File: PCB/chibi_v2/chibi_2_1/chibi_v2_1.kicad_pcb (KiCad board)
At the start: 2 copper layers, 43.8 x 94 mm, 13 parts, among them J2 Conn_01x08_Pin, Q1 NPN, Q2 NPN, Q3 NPN, U1 Pico

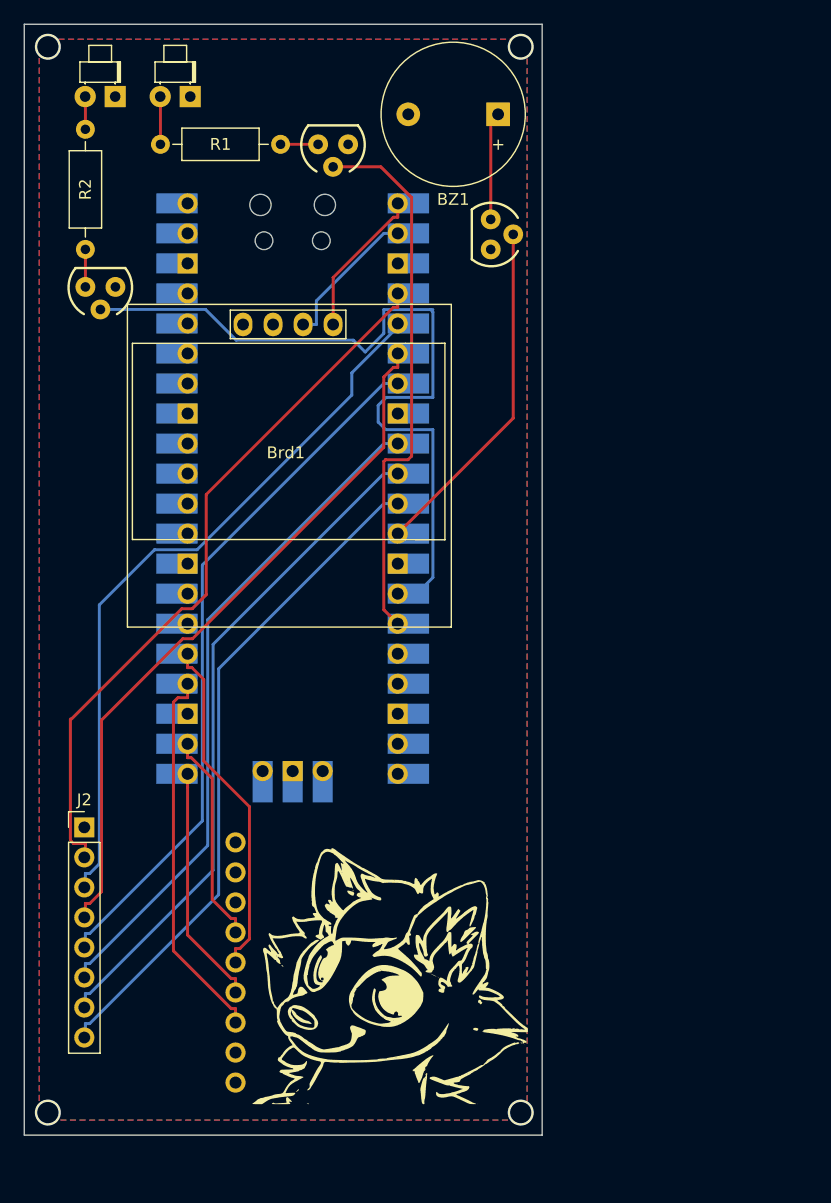
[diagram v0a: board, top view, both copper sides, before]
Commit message: PCB update, clearance issues solved (?)
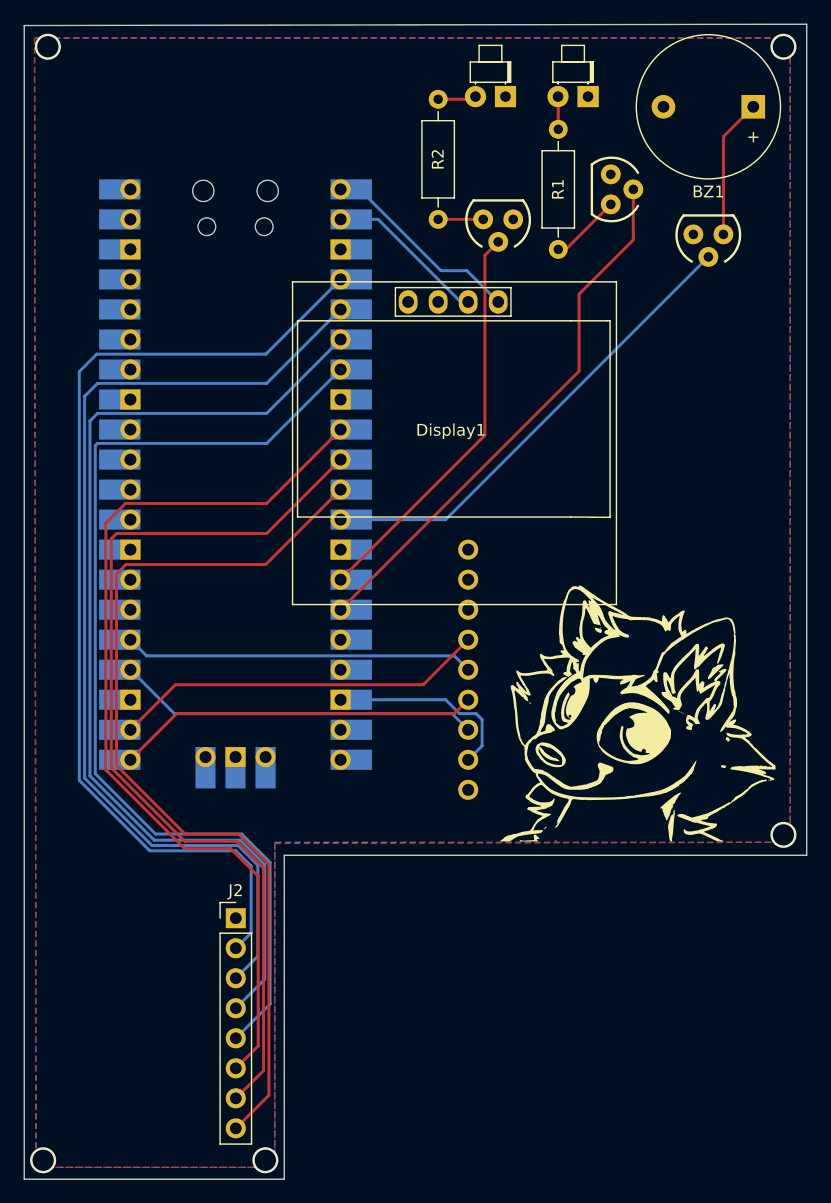
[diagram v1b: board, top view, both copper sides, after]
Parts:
- moved Q2 34.1 mm to (139.7, 50.8)
- moved D2 33.7 mm to (147.3, 40.4)
- moved D1 33.0 mm to (140.3, 40.4)
- moved SDCard1 31.6 mm to (146.6, 88.2)
- moved G*** 30.5 mm to (151.1, 92.1)
- moved R2 30.0 mm to (134.6, 50.8)
- moved R1 25.1 mm to (144.8, 53.3), turned to 90 degrees
- moved Q3 23.8 mm to (149.2, 48.3), turned to -90 degrees
- moved BZ1 21.6 mm to (161.3, 41.3)
- moved Q1 18.4 mm to (157.5, 52.1), turned to 180 degrees
- moved J2 14.9 mm to (117.5, 109.9)
- moved Display1 14.1 mm to (135.7, 68.4)
- moved Pico1 4.98 mm to (117.5, 72.4)
- renumbered Brd1 to Display1, U1 to Pico1, U2 to SDCard1
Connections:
- J2 pad 1: GND -> +3V3
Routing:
- net Net-(Pico1-GPIO10): track 67.1 -> 34.1 mm
- net Net-(J2-Pin_5): track 59.6 -> 85.2 mm
- net Net-(J2-Pin_4): track 59.6 -> 85.2 mm
- net Net-(J2-Pin_3): track 61.0 -> 85.0 mm
- net Net-(J2-Pin_2): track 60.9 -> 84.9 mm
- net Net-(J2-Pin_7): track 57.0 -> 78.4 mm
- net Net-(J2-Pin_8): track 57.0 -> 78.0 mm
- net Net-(J2-Pin_6): track 57.0 -> 77.7 mm
- net GND: track 0.00 -> 16.6 mm
- net Net-(Pico1-GPIO17): track 18.0 -> 31.7 mm
- net Net-(Pico1-GPIO9): track 29.4 -> 40.3 mm
- net Net-(Pico1-GPIO16): track 20.4 -> 30.7 mm
- net Net-(Display1-SDA): track 12.7 -> 17.3 mm
- net Net-(Q3-C): track 3.17 -> 6.02 mm
- net Net-(BZ1-+): track 9.15 -> 11.8 mm
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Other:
- board size 43.8 x 94 mm -> 66.2 x 97.7 mm

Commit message: Cosmetic change, gbr + drl files generated
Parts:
- moved G*** 2.22 mm to (151.4, 89.9)
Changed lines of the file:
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@@
   )
   (footprint "LOGO" (layer "F.Cu")
-    (at 151.13 92.075)
+    (at 151.426471 89.8764)
     (attr board_only exclude_from_pos_files exclude_from_bom)
     (fp_text reference "G***" (at 0 0) (layer "F.SilkS") hide

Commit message: charging pins, grb + drl files added
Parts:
- added J1: Conn_01x02, Connector_PinHeader_2.54mm:PinHeader_1x02_P2.54mm_Vertical, F.Cu at (105.9, 42.6)
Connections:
- Pico1 pad 40: unconnected-(Pico1-VBUS-Pad40) -> Net-(J1-Pin_2)
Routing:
- net Net-(J1-Pin_2): track 0.00 -> 5.71 mm
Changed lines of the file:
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@@
       (drillshape 0)
       (scaleselection 1)
-      (outputdirectory "output/")
+      (outputdirectory "../output/")
     )
   )
@@
   (net 37 "unconnected-(Pico1-3V3_EN-Pad37)")
   (net 38 "unconnected-(Pico1-VSYS-Pad39)")
-  (net 39 "unconnected-(Pico1-VBUS-Pad40)")
+  (net 39 "Net-(J1-Pin_2)")
   (net 40 "unconnected-(Pico1-SWCLK-Pad41)")
   (net 41 "unconnected-(Pico1-GND-Pad42)")
@@
       (net 4 "Net-(Display1-SDA)") (pinfunction "SDA") (pintype "input"))
   )
+  (footprint "Connector_PinHeader_2.54mm:PinHeader_1x02_P2.54mm_Vertical" (layer "F.Cu")
+    (at 105.925 42.6 90)
+    (descr "Through hole straight pin header, 1x02, 2.54mm pitch, single row")
+    (tags "Through hole pin header THT 1x02 2.54mm single row")
+    (property "Sheetfile" "chibi_v2_1.kicad_sch")
+    (property "Sheetname" "")
+    (property "ki_description" "Generic connector, single row, 01x02, script generated (kicad-library-utils/schlib/autogen/connector/)")
+    (property "ki_keywords" "connector")
+    (attr through_hole)
+    (fp_text reference "J1" (at 0 -2.33 90) (layer "F.SilkS") hide
+        (effects (font (size 1 1) (thickness 0.15)))
+    )
+    (fp_text value "Conn_01x02" (at 0 4.87 90) (layer "F.Fab")
+        (effects (font (size 1 1) (thickness 0.15)))
+    )
+    (fp_text user "${REFERENCE}" (at 0 1.27) (layer "F.Fab")
+        (effects (font (size 1 1) (thickness 0.15)))
+    )
+    (fp_line (start -1.33 -1.33) (end 0 -1.33)
+      (stroke (width 0.12) (type solid)) (layer "F.SilkS"))
+    (fp_line (start -1.33 0) (end -1.33 -1.33)
+      (stroke (width 0.12) (type solid)) (layer "F.SilkS"))
+    (fp_line (start -1.33 1.27) (end -1.33 3.87)
+      (stroke (width 0.12) (type solid)) (layer "F.SilkS"))
+    (fp_line (start -1.33 1.27) (end 1.33 1.27)
+      (stroke (width 0.12) (type solid)) (layer "F.SilkS"))
+    (fp_line (start -1.33 3.87) (end 1.33 3.87)
+      (stroke (width 0.12) (type solid)) (layer "F.SilkS"))
+    (fp_line (start 1.33 1.27) (end 1.33 3.87)
+      (stroke (width 0.12) (type solid)) (layer "F.SilkS"))
+    (fp_line (start -1.8 -1.8) (end -1.8 4.35)
+      (stroke (width 0.05) (type solid)) (layer "F.CrtYd"))
+    (fp_line (start -1.8 4.35) (end 1.8 4.35)
+      (stroke (width 0.05) (type solid)) (layer "F.CrtYd"))
+    (fp_line (start 1.8 -1.8) (end -1.8 -1.8)
+      (stroke (width 0.05) (type solid)) (layer "F.CrtYd"))
+    (fp_line (start 1.8 4.35) (end 1.8 -1.8)
+      (stroke (width 0.05) (type solid)) (layer "F.CrtYd"))
+    (fp_line (start -1.27 -0.635) (end -0.635 -1.27)
+      (stroke (width 0.1) (type solid)) (layer "F.Fab"))
+    (fp_line (start -1.27 3.81) (end -1.27 -0.635)
+      (stroke (width 0.1) (type solid)) (layer "F.Fab"))
+    (fp_line (start -0.635 -1.27) (end 1.27 -1.27)
+      (stroke (width 0.1) (type solid)) (layer "F.Fab"))
+    (fp_line (start 1.27 -1.27) (end 1.27 3.81)
+      (stroke (width 0.1) (type solid)) (layer "F.Fab"))
+    (fp_line (start 1.27 3.81) (end -1.27 3.81)
+      (stroke (width 0.1) (type solid)) (layer "F.Fab"))
+    (pad "1" thru_hole rect (at 0 0 90) (size 1.7 1.7) (drill 1) (layers "*.Cu" "*.Mask")
+      (net 1 "GND") (pinfunction "Pin_1") (pintype "passive"))
+    (pad "2" thru_hole oval (at 0 2.54 90) (size 1.7 1.7) (drill 1) (layers "*.Cu" "*.Mask")
+      (net 39 "Net-(J1-Pin_2)") (pinfunction "Pin_2") (pintype "passive"))
+    (model "${KICAD6_3DMODEL_DIR}/Connector_PinHeader_2.54mm.3dshapes/PinHeader_1x02_P2.54mm_Vertical.wrl"
+      (offset (xyz 0 0 0))
+      (scale (xyz 1 1 1))
+      (rotate (xyz 0 0 0))
+    )
+  )
   (footprint "LOGO" (layer "F.Cu")
     (at 151.426471 89.8764)
@@
       (net 38 "unconnected-(Pico1-VSYS-Pad39)") (pinfunction "VSYS") (pintype "power_in"))
     (pad "40" thru_hole oval (at 8.89 24.13 180) (size 1.7 1.7) (drill 1.02) (layers "*.Cu" "*.Mask")
-      (net 39 "unconnected-(Pico1-VBUS-Pad40)") (pinfunction "VBUS") (pintype "power_in"))
+      (net 39 "Net-(J1-Pin_2)") (pinfunction "VBUS") (pintype "power_in"))
     (pad "40" smd rect (at 8.89 24.13 180) (size 3.5 1.7) (drill (offset 0.9 0)) (layers "B.Cu" "B.Mask")
-      (net 39 "unconnected-(Pico1-VBUS-Pad40)") (pinfunction "VBUS") (pintype "power_in"))
+      (net 39 "Net-(J1-Pin_2)") (pinfunction "VBUS") (pintype "power_in"))
     (pad "41" thru_hole oval (at -2.54 -23.9 180) (size 1.7 1.7) (drill 1.02) (layers "*.Cu" "*.Mask")
       (net 40 "unconnected-(Pico1-SWCLK-Pad41)") (pinfunction "SWCLK") (pintype "input"))
@@
   (segment (start 137.16 88.9) (end 135.985 87.725) (width 0.25) (layer "B.Cu") (net 26))
   (segment (start 135.985 87.725) (end 109.95 87.725) (width 0.25) (layer "B.Cu") (net 26))
+  (segment (start 108.465 42.6) (end 108.465 48.14) (width 0.25) (layer "F.Cu") (net 39))
+  (segment (start 108.465 48.14) (end 108.585 48.26) (width 0.25) (layer "F.Cu") (net 39))
   (segment (start 138.43 50.8) (end 134.62 50.8) (width 0.25) (layer "F.Cu") (net 46))
   (segment (start 145.415 53.34) (end 144.78 53.34) (width 0.25) (layer "F.Cu") (net 47))

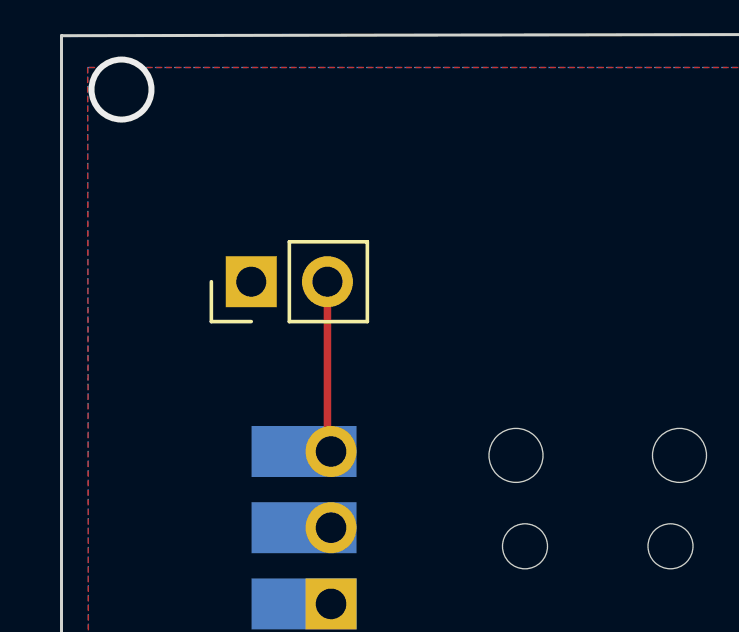
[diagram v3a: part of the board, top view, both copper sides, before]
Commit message: power pins added
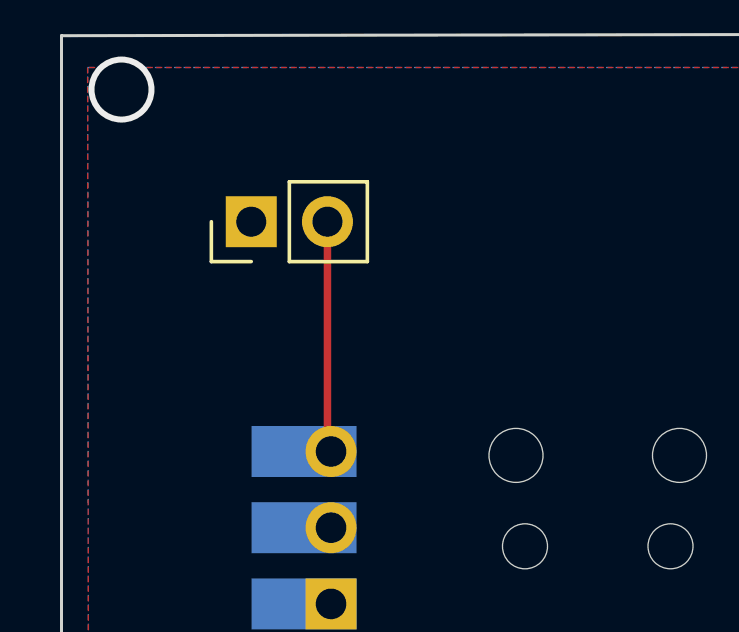
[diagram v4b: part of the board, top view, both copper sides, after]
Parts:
- moved J1 2.00 mm to (105.9, 40.6)
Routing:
- net Net-(J1-Pin_2): track 5.71 -> 7.71 mm
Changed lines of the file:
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@@
       (drillshape 0)
       (scaleselection 1)
-      (outputdirectory "../output/")
+      (outputdirectory "export/")
     )
   )
@@
   )
   (footprint "Connector_PinHeader_2.54mm:PinHeader_1x02_P2.54mm_Vertical" (layer "F.Cu")
-    (at 105.925 42.6 90)
+    (at 105.925 40.6 90)
     (descr "Through hole straight pin header, 1x02, 2.54mm pitch, single row")
     (tags "Through hole pin header THT 1x02 2.54mm single row")
@@
   (segment (start 137.16 88.9) (end 135.985 87.725) (width 0.25) (layer "B.Cu") (net 26))
   (segment (start 135.985 87.725) (end 109.95 87.725) (width 0.25) (layer "B.Cu") (net 26))
-  (segment (start 108.465 42.6) (end 108.465 48.14) (width 0.25) (layer "F.Cu") (net 39))
   (segment (start 108.465 48.14) (end 108.585 48.26) (width 0.25) (layer "F.Cu") (net 39))
+  (segment (start 108.465 40.6) (end 108.465 48.14) (width 0.25) (layer "F.Cu") (net 39))
   (segment (start 138.43 50.8) (end 134.62 50.8) (width 0.25) (layer "F.Cu") (net 46))
   (segment (start 145.415 53.34) (end 144.78 53.34) (width 0.25) (layer "F.Cu") (net 47))

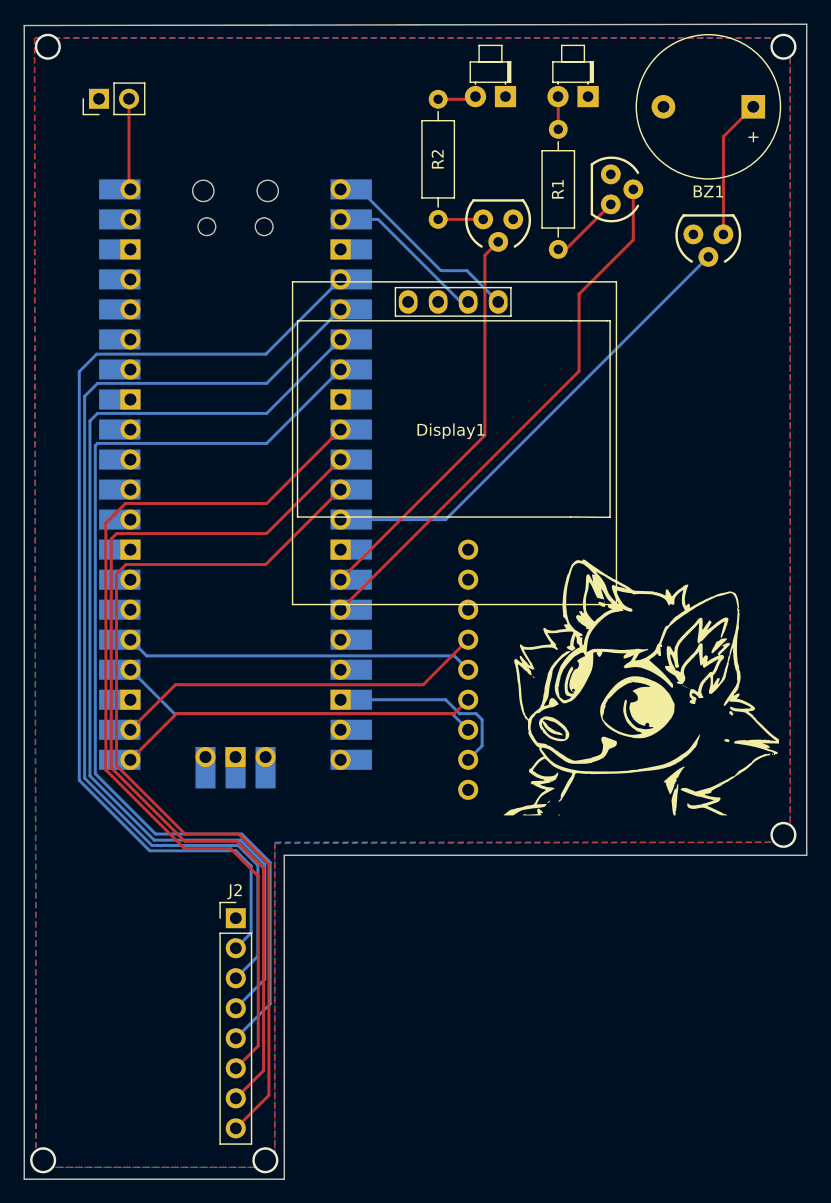
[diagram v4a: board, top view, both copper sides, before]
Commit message: repositioning of a few components in PCB V2.1
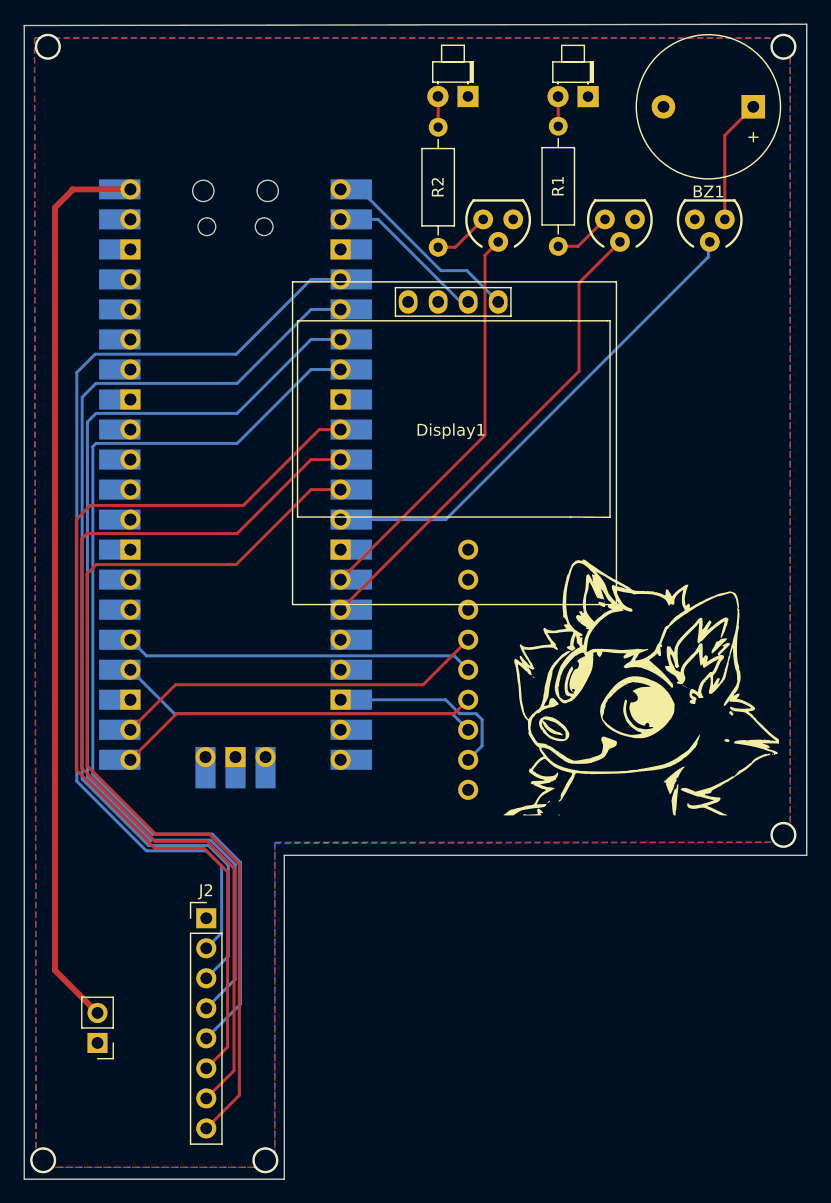
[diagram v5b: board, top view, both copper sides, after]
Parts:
- moved J1 79.9 mm to (105.8, 120.5), turned to 180 degrees
- moved D1 3.18 mm to (137.1, 40.4)
- moved Q3 2.66 mm to (150.0, 50.8), turned to 180 degrees
- moved J2 2.50 mm to (115.0, 109.9)
- moved R2 2.36 mm to (134.6, 53.2)
- moved Q1 1.28 mm to (157.6, 50.8)
- moved R1 0.26 mm to (144.8, 53.1)
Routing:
- net Net-(J1-Pin_2): track 7.71 -> 76.7 mm
- net Net-(Pico1-GPIO11): track 45.8 -> 40.9 mm
- net Net-(J2-Pin_6): track 77.7 -> 80.4 mm
- net Net-(J2-Pin_8): track 78.0 -> 80.5 mm
- net Net-(J2-Pin_7): track 78.4 -> 80.9 mm
- net Net-(J2-Pin_4): track 85.2 -> 83.0 mm
- net Net-(J2-Pin_5): track 85.2 -> 83.0 mm
- net Net-(J2-Pin_3): track 85.0 -> 82.9 mm
- net Net-(J2-Pin_2): track 84.9 -> 82.8 mm
- net Net-(Pico1-GPIO9): track 40.3 -> 41.6 mm
- net Net-(BZ1-+): track 11.8 -> 10.5 mm
- net Net-(Q3-C): track 6.02 -> 4.89 mm
- net Net-(Q2-C): track 3.81 -> 4.79 mm
- net Net-(D1-A): track 3.25 -> 2.64 mm
